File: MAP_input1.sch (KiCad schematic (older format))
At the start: 4 parts, among them U6 MPX4100A

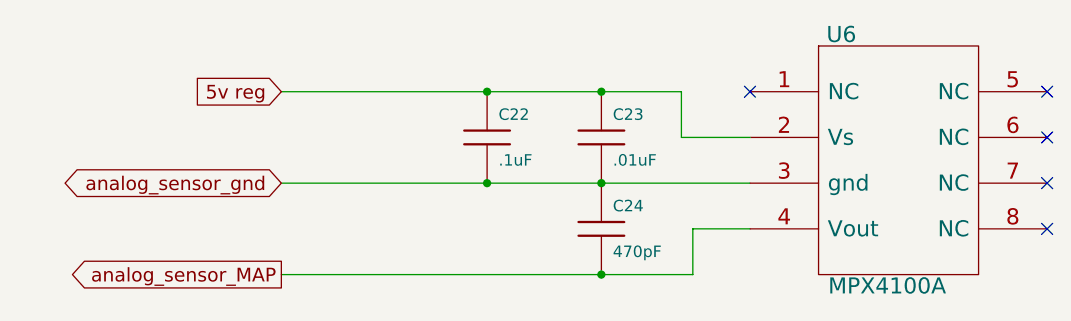
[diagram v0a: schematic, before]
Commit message: Removed LM1815 options. Now adaptive mode and square waves are the default,
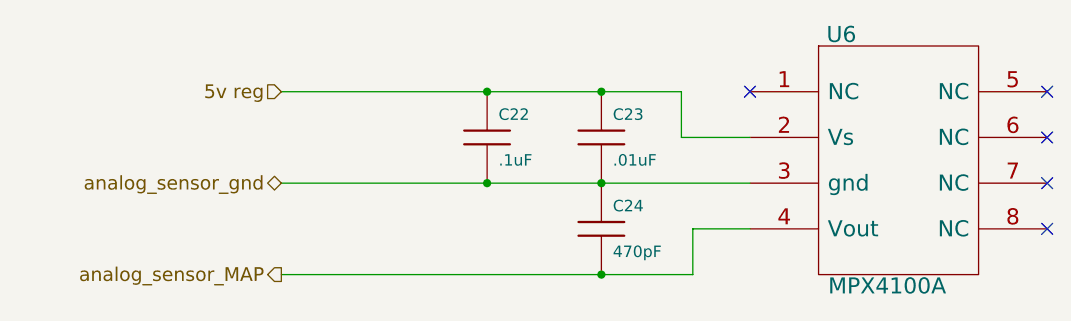
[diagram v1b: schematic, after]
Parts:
- C22: Field1 (none) -> newark,97M4164; Field2 (none) -> vendor1, smd w hem; Field3 (none) -> vendor2, thru w hem; Field4 (none) -> vendor2, smd w hem; Field5 (none) -> 50,V; Field6 (none) -> 10,%; Field7 (none) -> multilayer ceramic; Field8 (none) -> other,more,stuff
- C23: Field1 (none) -> newark,75M7682; Field2 (none) -> vendor1, smd w hem; Field3 (none) -> vendor2, thru w hem; Field4 (none) -> vendor2, smd w hem; Field5 (none) -> 50,V; Field6 (none) -> 10,%; Field7 (none) -> multilayer ceramic; Field8 (none) -> other,more,stuff
- C24: Field1 (none) -> newark,19C6191; Field2 (none) -> vendor1, smd w hem; Field3 (none) -> vendor2, thru w hem; Field4 (none) -> vendor2, smd w hem; Field5 (none) -> 100,V; Field6 (none) -> 5,%; Field7 (none) -> multilayer ceramic; Field8 (none) -> other,more,stuff
- U6: Field1 (none) -> newark,75C3857; Field2 (none) -> vendor1, smd w hem; Field3 (none) -> vendor2, thru w hem; Field4 (none) -> vendor2, smd w hem; Field5 (none) -> x,x; Field6 (none) -> x,x; Field7 (none) -> x; Field8 (none) -> other,more,stuff
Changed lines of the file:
@@
-EESchema Schematic File Version 1
-LIBS:power,./freeEMS_lib,device,conn,linear,regul,74xx,cmos4000,adc-dac,memory,xilinx,special,microcontrollers,dsp,microchip,analog_switches,motorola,texas,intel,audio,interface,digital-audio,philips,display,cypress,siliconi,contrib,valves,./freeEMS_1.cache
+EESchema Schematic File Version 2  date Fri 02 Jul 2010 02:24:35 PM ART
+LIBS:power
+LIBS:freeEMS_lib
+LIBS:device
+LIBS:conn
+LIBS:linear
+LIBS:regul
+LIBS:74xx
+LIBS:cmos4000
+LIBS:adc-dac
+LIBS:memory
+LIBS:xilinx
+LIBS:special
+LIBS:microcontrollers
+LIBS:dsp
+LIBS:microchip
+LIBS:analog_switches
+LIBS:motorola
+LIBS:texas
+LIBS:intel
+LIBS:audio
+LIBS:interface
+LIBS:digital-audio
+LIBS:philips
+LIBS:display
+LIBS:cypress
+LIBS:siliconi
+LIBS:contrib
+LIBS:valves
+LIBS:freeEMS_1-cache
 EELAYER 23  0
 EELAYER END
@@
 Sheet 17 41
 Title "freeEMS 1.0"
-Date "15 nov 2008"
+Date "2 jul 2010"
 Rev "A.20"
 Comp "diyefi.org"
@@
 U 1 1 48B144B7
 P 5100 1500
-F 0 "U6" H 4850 2050 70  0000 C C
-F 1 "MPX4100A" H 5050 950 70  0000 C C
-F 2 "SOP_case_482" V 1130 2600 60  0001 C C
-F 4 "newark,75C3857" V 1130 2600 60  0001 C C
-F 5 "vendor1, smd w hem" V 1130 2600 60  0001 C C
-F 6 "vendor2, thru w hem" V 1130 2600 60  0001 C C
-F 7 "vendor2, smd w hem" V 1130 2600 60  0001 C C
-F 8 "x,x" V 1130 2600 60  0001 C C
-F 9 "x,x" V 1130 2600 60  0001 C C
-F 10 "x" V 1130 2600 60  0001 C C
-F 11 "other,more,stuff" V 1130 2600 60  0001 C C
+F 0 "U6" H 4850 2050 70  0000 C CNN
+F 1 "MPX4100A" H 5050 950 70  0000 C CNN
+F 2 "SOP_case_482" V 1130 2600 60  0001 C CNN
+F 4 "newark,75C3857" V 1130 2600 60  0001 C CNN "Field1"
+F 5 "vendor1, smd w hem" V 1130 2600 60  0001 C CNN "Field2"
+F 6 "vendor2, thru w hem" V 1130 2600 60  0001 C CNN "Field3"
+F 7 "vendor2, smd w hem" V 1130 2600 60  0001 C CNN "Field4"
+F 8 "x,x" V 1130 2600 60  0001 C CNN "Field5"
+F 9 "x,x" V 1130 2600 60  0001 C CNN "Field6"
+F 10 "x" V 1130 2600 60  0001 C CNN "Field7"
+F 11 "other,more,stuff" V 1130 2600 60  0001 C CNN "Field8"
 	1    5100 1500
 	1    0    0    -1
@@
 Wire Wire Line
 	4150 1400 4150 1200
-Text GLabel 2400 1600 0    60   BiDi
+Text HLabel 2400 1600 0    60   BiDi ~ 0
 analog_sensor_gnd
 $Comp
@@
 U 1 1 488D2158
 P 3800 1400
-F 0 "C23" H 3850 1500 50  0000 L C
-F 1 ".01uF" H 3850 1300 50  0000 L C
-F 2 "C1V7" V 1130 2600 60  0001 C C
-F 4 "newark,75M7682" V 1130 2600 60  0001 C C
-F 5 "vendor1, smd w hem" V 1130 2600 60  0001 C C
-F 6 "vendor2, thru w hem" V 1130 2600 60  0001 C C
-F 7 "vendor2, smd w hem" V 1130 2600 60  0001 C C
-F 8 "50,V" V 1130 2600 60  0001 C C
-F 9 "10,%" V 1130 2600 60  0001 C C
-F 10 "multilayer ceramic" V 1130 2600 60  0001 C C
-F 11 "other,more,stuff" V 1130 2600 60  0001 C C
+F 0 "C23" H 3850 1500 50  0000 L CNN
+F 1 ".01uF" H 3850 1300 50  0000 L CNN
+F 2 "C1V7" V 1130 2600 60  0001 C CNN
+F 4 "newark,75M7682" V 1130 2600 60  0001 C CNN "Field1"
+F 5 "vendor1, smd w hem" V 1130 2600 60  0001 C CNN "Field2"
+F 6 "vendor2, thru w hem" V 1130 2600 60  0001 C CNN "Field3"
+F 7 "vendor2, smd w hem" V 1130 2600 60  0001 C CNN "Field4"
+F 8 "50,V" V 1130 2600 60  0001 C CNN "Field5"
+F 9 "10,%" V 1130 2600 60  0001 C CNN "Field6"
+F 10 "multilayer ceramic" V 1130 2600 60  0001 C CNN "Field7"
+F 11 "other,more,stuff" V 1130 2600 60  0001 C CNN "Field8"
 	1    3800 1400
 	1    0    0    -1
@@
 U 1 1 488D2153
 P 3800 1800
-F 0 "C24" H 3850 1900 50  0000 L C
-F 1 "470pF" H 3850 1700 50  0000 L C
-F 2 "C1V7" V 1130 2600 60  0001 C C
-F 4 "newark,19C6191" V 1130 2600 60  0001 C C
-F 5 "vendor1, smd w hem" V 1130 2600 60  0001 C C
-F 6 "vendor2, thru w hem" V 1130 2600 60  0001 C C
-F 7 "vendor2, smd w hem" V 1130 2600 60  0001 C C
-F 8 "100,V" V 1130 2600 60  0001 C C
-F 9 "5,%" V 1130 2600 60  0001 C C
-F 10 "multilayer ceramic" V 1130 2600 60  0001 C C
-F 11 "other,more,stuff" V 1130 2600 60  0001 C C
+F 0 "C24" H 3850 1900 50  0000 L CNN
+F 1 "470pF" H 3850 1700 50  0000 L CNN
+F 2 "C1V7" V 1130 2600 60  0001 C CNN
+F 4 "newark,19C6191" V 1130 2600 60  0001 C CNN "Field1"
+F 5 "vendor1, smd w hem" V 1130 2600 60  0001 C CNN "Field2"
+F 6 "vendor2, thru w hem" V 1130 2600 60  0001 C CNN "Field3"
+F 7 "vendor2, smd w hem" V 1130 2600 60  0001 C CNN "Field4"
+F 8 "100,V" V 1130 2600 60  0001 C CNN "Field5"
+F 9 "5,%" V 1130 2600 60  0001 C CNN "Field6"
+F 10 "multilayer ceramic" V 1130 2600 60  0001 C CNN "Field7"
+F 11 "other,more,stuff" V 1130 2600 60  0001 C CNN "Field8"
 	1    3800 1800
 	1    0    0    -1
@@
 U 1 1 488D2133
 P 3300 1400
-F 0 "C22" H 3350 1500 50  0000 L C
-F 1 ".1uF" H 3350 1300 50  0000 L C
-F 2 "C1V7" V 1130 2600 60  0001 C C
-F 4 "newark,97M4164" V 1130 2600 60  0001 C C
-F 5 "vendor1, smd w hem" V 1130 2600 60  0001 C C
-F 6 "vendor2, thru w hem" V 1130 2600 60  0001 C C
-F 7 "vendor2, smd w hem" V 1130 2600 60  0001 C C
-F 8 "50,V" V 1130 2600 60  0001 C C
-F 9 "10,%" V 1130 2600 60  0001 C C
-F 10 "multilayer ceramic" V 1130 2600 60  0001 C C
-F 11 "other,more,stuff" V 1130 2600 60  0001 C C
+F 0 "C22" H 3350 1500 50  0000 L CNN
+F 1 ".1uF" H 3350 1300 50  0000 L CNN
+F 2 "C1V7" V 1130 2600 60  0001 C CNN
+F 4 "newark,97M4164" V 1130 2600 60  0001 C CNN "Field1"
+F 5 "vendor1, smd w hem" V 1130 2600 60  0001 C CNN "Field2"
+F 6 "vendor2, thru w hem" V 1130 2600 60  0001 C CNN "Field3"
+F 7 "vendor2, smd w hem" V 1130 2600 60  0001 C CNN "Field4"
+F 8 "50,V" V 1130 2600 60  0001 C CNN "Field5"
+F 9 "10,%" V 1130 2600 60  0001 C CNN "Field6"
+F 10 "multilayer ceramic" V 1130 2600 60  0001 C CNN "Field7"
+F 11 "other,more,stuff" V 1130 2600 60  0001 C CNN "Field8"
 	1    3300 1400
 	1    0    0    -1
 $EndComp
-Text GLabel 2400 1200 0    60   Input
+Text HLabel 2400 1200 0    60   Input ~ 0
 5v reg
-Text GLabel 2400 2000 0    60   Output
+Text HLabel 2400 2000 0    60   Output ~ 0
 analog_sensor_MAP
 $EndSCHEMATC

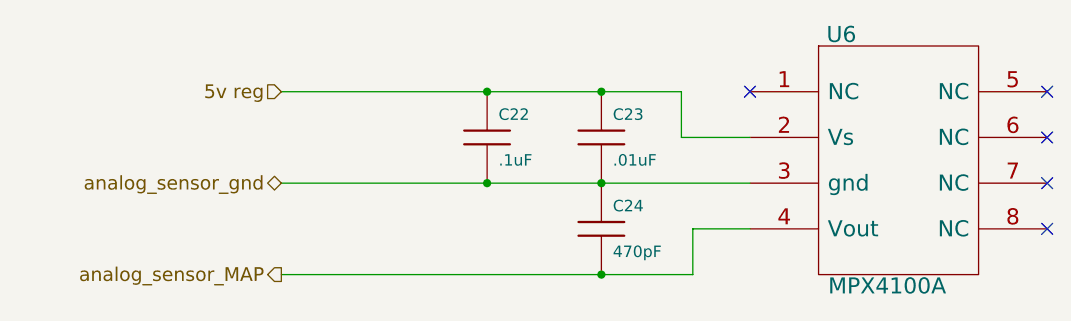
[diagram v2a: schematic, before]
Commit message: Implemented P&H, removed current sense circuitry, removed all unnecessary files from the repo
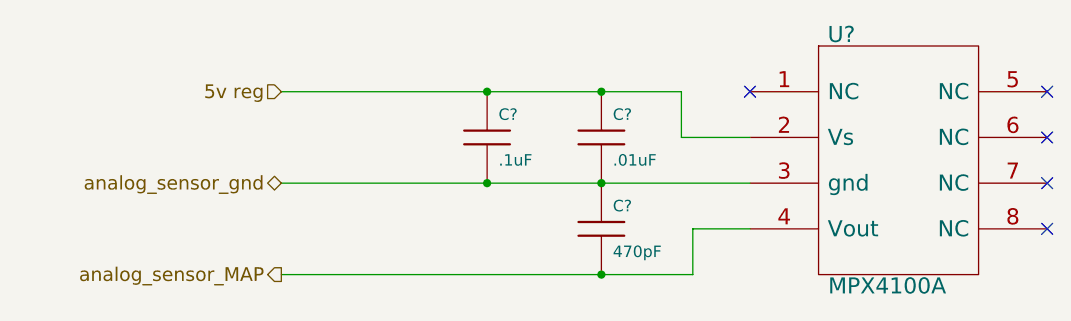
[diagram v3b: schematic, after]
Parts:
- renumbered C22 to C?, C24 to C?, C23 to C?, U6 to U?
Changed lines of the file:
@@
-EESchema Schematic File Version 2  date Fri 02 Jul 2010 05:44:26 PM ART
+EESchema Schematic File Version 2  date Sat 03 Jul 2010 10:49:02 AM ART
 LIBS:power
 LIBS:freeEMS_lib
@@
 EELAYER END
 $Descr A 11000 8500
-Sheet 17 41
+Sheet 1 41
 Title "freeEMS 1.0"
-Date "2 jul 2010"
-Rev "A.20"
+Date "3 jul 2010"
+Rev "A.07"
 Comp "diyefi.org"
 Comment1 "MAP_input.sch"
@@
 $EndDescr
 $Comp
-L MPX4100A U6
+L MPX4100A U?
 U 1 1 48B144B7
 P 5100 1500
-F 0 "U6" H 4850 2050 70  0000 C CNN
+F 0 "U?" H 4850 2050 70  0000 C CNN
 F 1 "MPX4100A" H 5050 950 70  0000 C CNN
 F 2 "SOP_case_482" V 1130 2600 60  0001 C CNN
@@
 analog_sensor_gnd
 $Comp
-L C C23
+L C C?
 U 1 1 488D2158
 P 3800 1400
-F 0 "C23" H 3850 1500 50  0000 L CNN
+F 0 "C?" H 3850 1500 50  0000 L CNN
 F 1 ".01uF" H 3850 1300 50  0000 L CNN
 F 2 "C1V7" V 1130 2600 60  0001 C CNN
@@
 $EndComp
 $Comp
-L C C24
+L C C?
 U 1 1 488D2153
 P 3800 1800
-F 0 "C24" H 3850 1900 50  0000 L CNN
+F 0 "C?" H 3850 1900 50  0000 L CNN
 F 1 "470pF" H 3850 1700 50  0000 L CNN
 F 2 "C1V7" V 1130 2600 60  0001 C CNN
@@
 $EndComp
 $Comp
-L C C22
+L C C?
 U 1 1 488D2133
 P 3300 1400
-F 0 "C22" H 3350 1500 50  0000 L CNN
+F 0 "C?" H 3350 1500 50  0000 L CNN
 F 1 ".1uF" H 3350 1300 50  0000 L CNN
 F 2 "C1V7" V 1130 2600 60  0001 C CNN
